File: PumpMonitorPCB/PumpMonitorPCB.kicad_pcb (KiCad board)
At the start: 2 copper layers, 103 parts, among them J1 Live terminals, J10 Aux GPIO 4, J2 Neutral terminals, J3 Mains terminals, J4 Auxilliary relay, J5 Debug, J6 USB_C_Receptacle_USB2.0_16P, J7 Aux GPIO 1, J8 Aux GPIO 2, J9 Aux GPIO 3, K1 J115F11CH5VDCS61-5U, K2 J115F11CH5VDCS61-5U, Q1 AS2302, Q2 AS2302, SW1 EN, SW2 LEFT, SW3 RIGHT, SW4 BOOT, U1 ACS770xCB-050B-PFF, U2 AMS1117-3.3, U3 LMV321, U4 LMV321, U5 ESP32-S3-WROOM-1, U6 MC14504B, U7 WIO-SX1262, U8 TPD3E001DRLR

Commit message: Added fuse on aux relay, setting creepage and clearance distances.
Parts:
- added F3: 10A, Fuse:Fuseholder_Cylinder-5x20mm_Stelvio-Kontek_PTF78_Horizontal_Open, F.Cu at (170.2, 170.4)
- moved J3 231.2 mm to (97.8, 196.8)
- moved J4 179.3 mm to (150.5, 196.8)
- moved TR1 146.0 mm to (125.4, 176.5)
- moved DS1 145.6 mm to (21.3, 96.4)
- moved K2 111.5 mm to (160.0, 176.6), turned to -90 degrees
- moved PS1 85.8 mm to (82.5, 176.5)
- moved F2 82.0 mm to (79.4, 186.7), turned to 0 degrees
- moved D3 72.5 mm to (148.2, 98.5)
- moved C8 72.5 mm to (139.7, 87.8)
- moved U2 72.5 mm to (140.5, 97.7)
- moved C1 72.5 mm to (139.7, 76.2)
- moved D2 72.5 mm to (148.2, 95.2)
- moved J8 56.4 mm to (250.2, 88.9)
- moved J7 56.0 mm to (233.7, 88.9)
- moved R23 22.5 mm to (223.5, 101.7), turned to 0 degrees
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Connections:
- K2 pad 11: /Main PCB/Aux common -> Net-(F3-Pad1)
- U1 pad 4: /Main PCB/Neutral out -> /Main PCB/Neutral in
- U1 pad 5: /Main PCB/Neutral in -> /Main PCB/Neutral out
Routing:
- net /Main PCB/Neutral in: track 190.4 -> 109.9 mm
- net /Main PCB/Live in: track 47.8 -> 88.9 mm
- net Net-(PS1-AC/L): track 58.5 -> 21.7 mm
- net /Main PCB/Aux NO: track 0.00 -> 26.5 mm
- net /Main PCB/Live out: track 45.3 -> 20.3 mm
- net Earth: track 16.5 -> 0.00 mm
- net /Main PCB/Aux NC: track 0.00 -> 15.7 mm
- net /Main PCB/Aux common: track 0.00 -> 13.0 mm
- net Net-(F3-Pad1): track 0.00 -> 12.7 mm
- net Net-(F1-Pad2): track 27.0 -> 15.0 mm
- net /Main PCB/Auxilliary connectors/AuxExt.4: track 0.00 -> 10.5 mm
- net /Main PCB/Auxilliary connectors/AuxExt.7: track 0.00 -> 10.2 mm
- net /Main PCB/Auxilliary connectors/Aux.7: track 0.00 -> 9.87 mm
- net /Main PCB/Auxilliary connectors/Aux.8: track 0.00 -> 9.87 mm
- net /Main PCB/Auxilliary connectors/Aux.4: track 0.00 -> 9.87 mm
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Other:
- board outline added: 337.8 x 228.6 mm

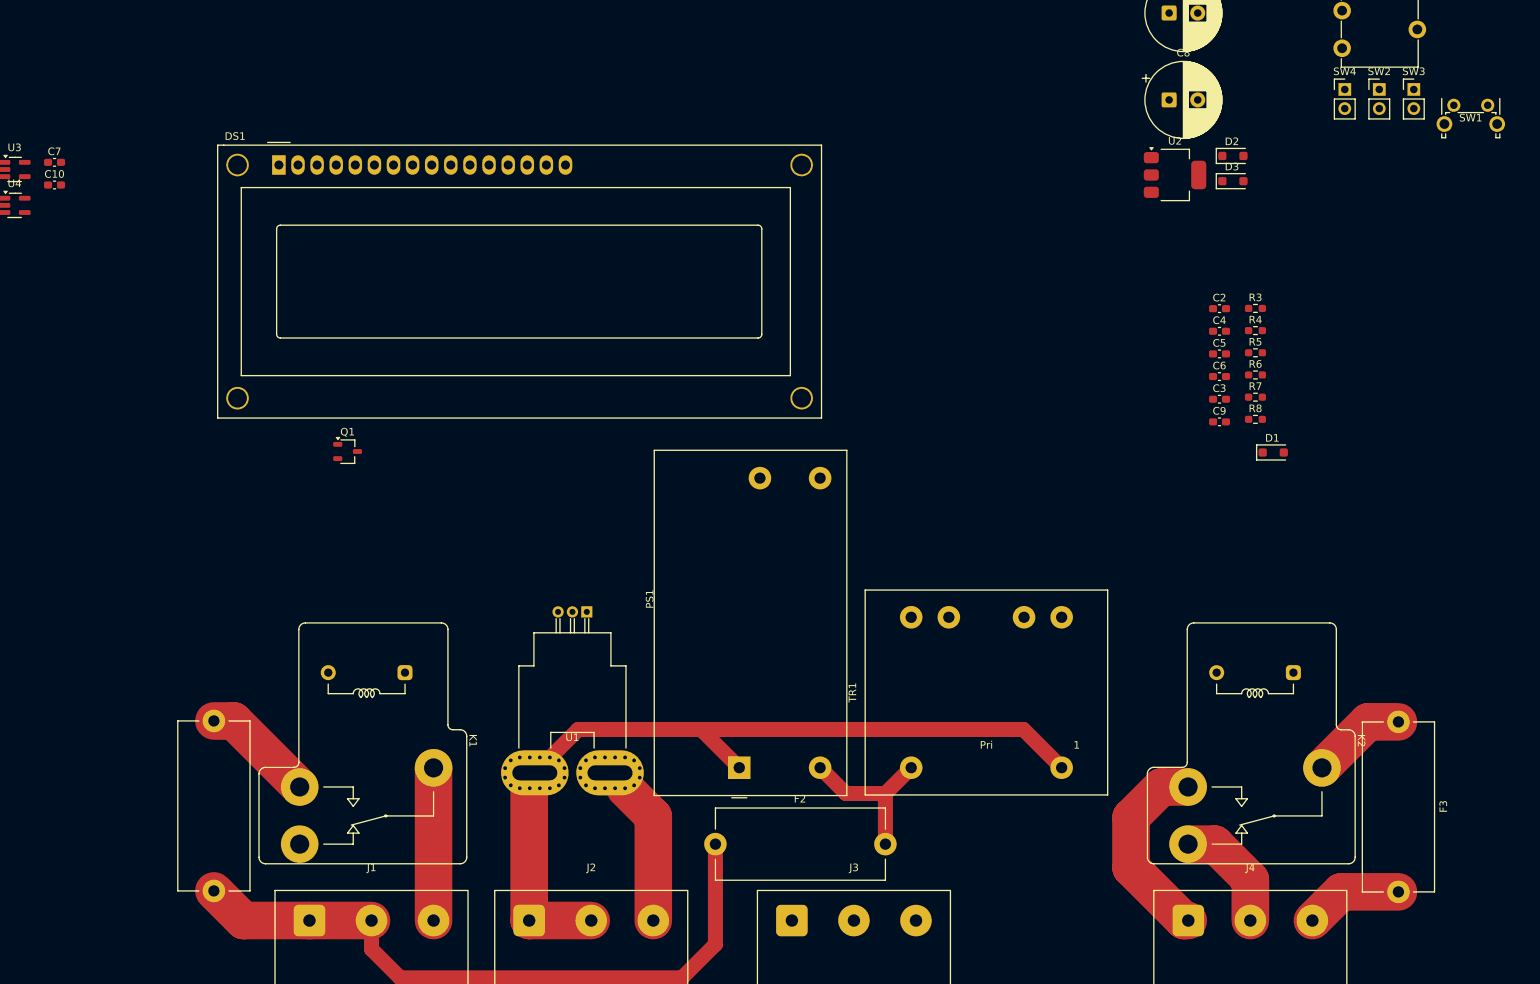
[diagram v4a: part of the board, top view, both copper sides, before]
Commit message: Adding test points, CAD files
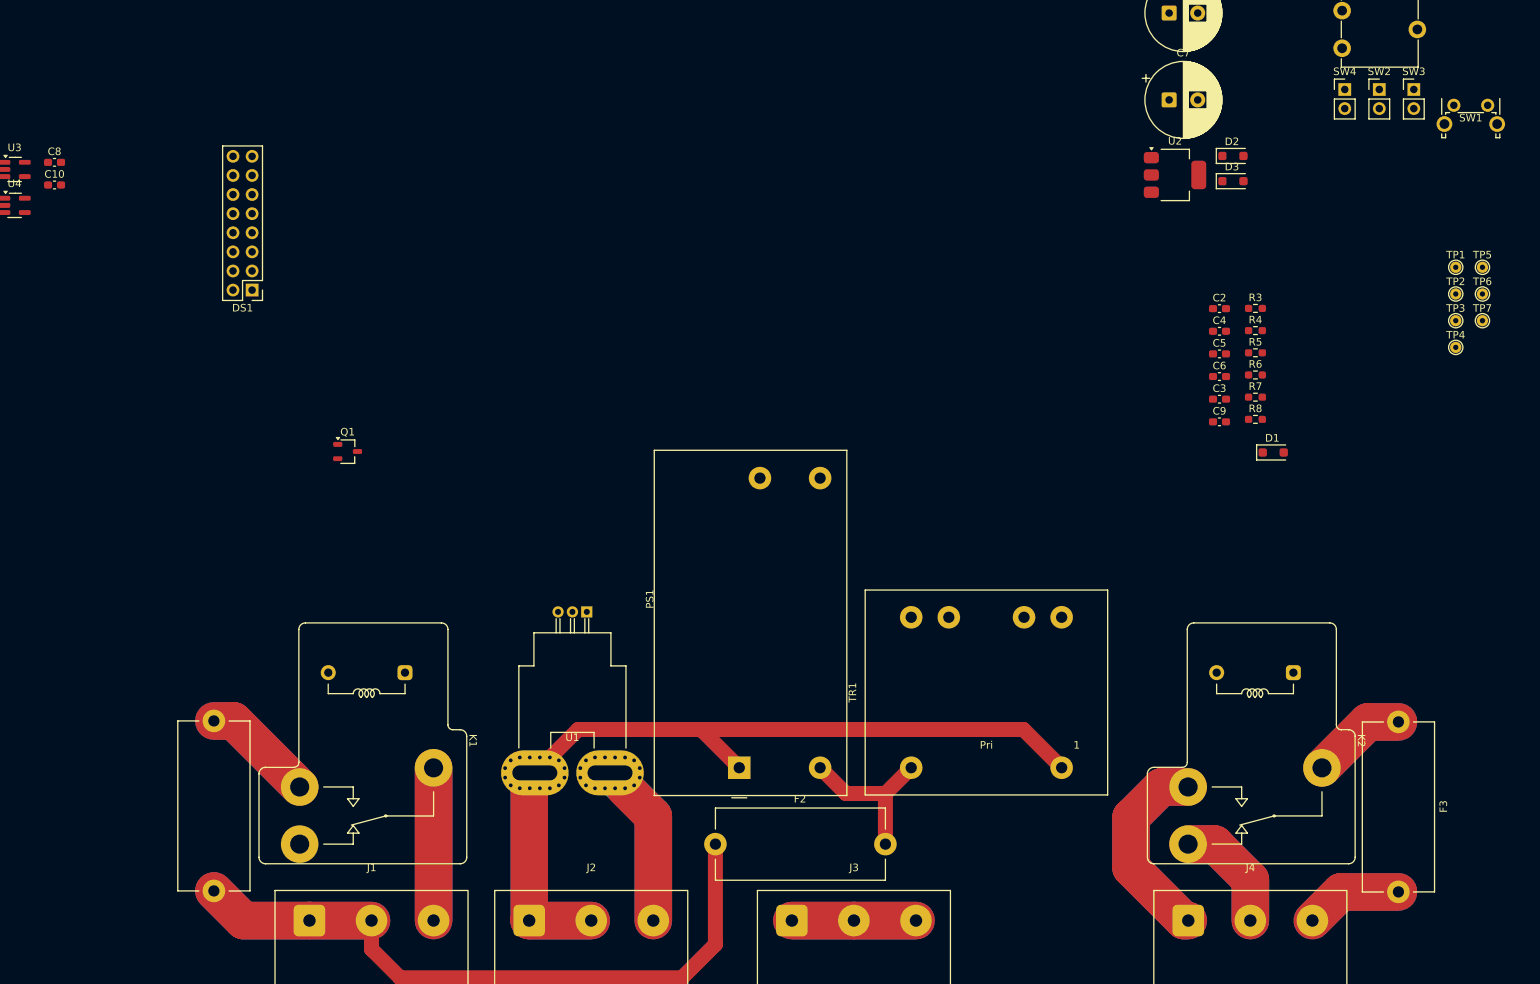
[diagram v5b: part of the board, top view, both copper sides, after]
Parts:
- added TP1: ~, TestPoint:TestPoint_THTPad_D1.5mm_Drill0.7mm, F.Cu at (177.8, 110.0)
- added TP2: ~, TestPoint:TestPoint_THTPad_D1.5mm_Drill0.7mm, F.Cu at (177.8, 113.5)
- added TP3: ~, TestPoint:TestPoint_THTPad_D1.5mm_Drill0.7mm, F.Cu at (177.8, 117.1)
- added TP4: ~, TestPoint:TestPoint_THTPad_D1.5mm_Drill0.7mm, F.Cu at (177.8, 120.7)
- added TP5: ~, TestPoint:TestPoint_THTPad_D1.5mm_Drill0.7mm, F.Cu at (181.4, 110.0)
- added TP6: ~, TestPoint:TestPoint_THTPad_D1.5mm_Drill0.7mm, F.Cu at (181.4, 113.5)
- added TP7: ~, TestPoint:TestPoint_THTPad_D1.5mm_Drill0.7mm, F.Cu at (181.4, 117.1)
- DS1: footprint Display:WC1602A -> Connector_PinHeader_2.54mm:PinHeader_2x08_P2.54mm_Vertical
- moved DS1 17.0 mm to (17.8, 113.0), turned to 180 degrees
- renumbered C8 to C7, C7 to C8
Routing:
- net Earth: track 0.00 -> 33.0 mm
- net /Main PCB/Neutral in: track 109.9 -> 138.1 mm
- net /Main PCB/Aux NO: track 26.5 -> 52.9 mm
- net /Main PCB/Live in: track 88.9 -> 111.5 mm
- net /Main PCB/Neutral out: track 19.1 -> 41.2 mm
- net /Main PCB/Live out: track 20.3 -> 40.6 mm
- net /Main PCB/Aux NC: track 15.7 -> 31.3 mm
- net Net-(F1-Pad2): track 15.0 -> 30.1 mm
- net /Main PCB/Aux common: track 13.0 -> 26.0 mm
- net Net-(F3-Pad1): track 12.7 -> 25.4 mm
